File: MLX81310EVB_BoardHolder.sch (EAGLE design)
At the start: 27 parts

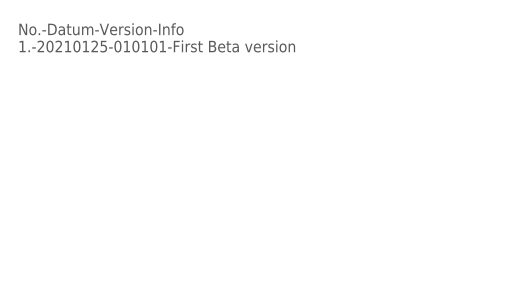
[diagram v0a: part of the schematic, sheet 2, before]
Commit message: Label added in SCH
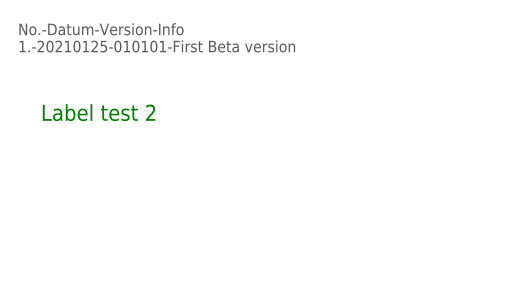
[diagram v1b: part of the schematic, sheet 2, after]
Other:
- note added: "Label test 2"
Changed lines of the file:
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@@
 6. HEX STANDOFF M3X0.5 BRASS 22MM
   DIGI-KEY -&gt; R30-1002202-ND</text>
+<text x="22.86" y="157.48" size="1.778" layer="91">Label test 2</text>
 </plain>
 <instances>

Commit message: test 4
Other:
- note added: "test 4"
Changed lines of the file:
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@@
   DIGI-KEY -&gt; R30-1002202-ND</text>
 <text x="22.86" y="157.48" size="1.778" layer="91">Label test 2</text>
+<text x="22.86" y="149.86" size="1.778" layer="91">test 4</text>
 </plain>
 <instances>
